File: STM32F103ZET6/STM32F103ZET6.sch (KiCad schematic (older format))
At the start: 0 parts

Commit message: git ignore STM32F103ZET6/STM32F103ZET6.sch-bak
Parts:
- added U?: STM32F103ZETx, Package_QFP:LQFP-144_20x20mm_P0.5mm, symbol MCU_ST_STM32F1:STM32F103ZETx
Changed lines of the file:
@@
 Comment4 ""
 $EndDescr
+$Comp
+L MCU_ST_STM32F1:STM32F103ZETx U?
+U 1 1 5E0CBF09
+P 5900 4000
+F 0 "U?" V 5854 357 50  0000 R CNN
+F 1 "STM32F103ZETx" V 5945 357 50  0000 R CNN
+F 2 "Package_QFP:LQFP-144_20x20mm_P0.5mm" H 4800 600 50  0001 R CNN
+F 3 "http://www.st.com/st-web-ui/static/active/en/resource/technical/document/datasheet/CD00191185.pdf" H 5900 4000 50  0001 C CNN
+	1    5900 4000
+	0    1    1    0
+$EndComp
 $EndSCHEMATC

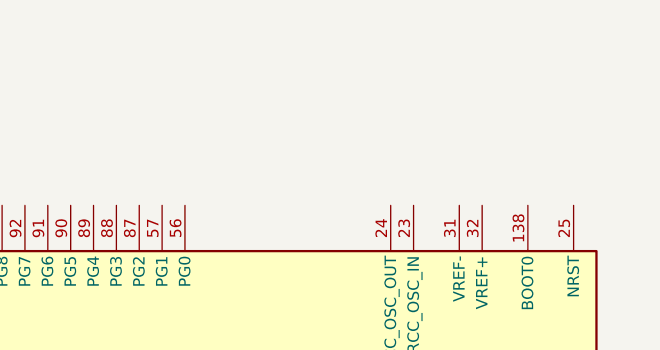
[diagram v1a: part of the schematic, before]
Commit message: remove STM32F103ZET6-cache.lib
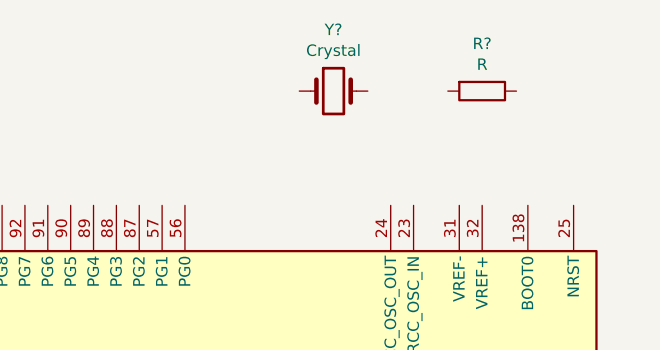
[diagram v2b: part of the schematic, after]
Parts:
- added R?: R, symbol Device:R
- added Y?: Crystal, symbol Device:Crystal
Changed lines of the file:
@@
 	0    1    1    0
 $EndComp
+$Comp
+L Device:R R?
+U 1 1 5E0CC0E2
+P 8800 2200
+F 0 "R?" V 8593 2200 50  0000 C CNN
+F 1 "R" V 8684 2200 50  0000 C CNN
+F 2 "" V 8730 2200 50  0001 C CNN
+F 3 "~" H 8800 2200 50  0001 C CNN
+	1    8800 2200
+	0    1    1    0
+$EndComp
+$Comp
+L Device:Crystal Y?
+U 1 1 5E0CC898
+P 8150 2200
+F 0 "Y?" H 8150 2468 50  0000 C CNN
+F 1 "Crystal" H 8150 2377 50  0000 C CNN
+F 2 "" H 8150 2200 50  0001 C CNN
+F 3 "~" H 8150 2200 50  0001 C CNN
+	1    8150 2200
+	1    0    0    -1
+$EndComp
 $EndSCHEMATC

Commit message: remove fp-info-cache
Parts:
- removed R?: R, symbol Device:R
- removed Y?: Crystal, symbol Device:Crystal
- gave numbers to parts that had none: 1
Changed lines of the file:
@@
 $EndDescr
 $Comp
-L MCU_ST_STM32F1:STM32F103ZETx U?
+L MCU_ST_STM32F1:STM32F103ZETx U1
 U 1 1 5E0CBF09
 P 5900 4000
-F 0 "U?" V 5854 357 50  0000 R CNN
+F 0 "U1" V 5854 357 50  0000 R CNN
 F 1 "STM32F103ZETx" V 5945 357 50  0000 R CNN
 F 2 "Package_QFP:LQFP-144_20x20mm_P0.5mm" H 4800 600 50  0001 R CNN
@@
 	0    1    1    0
 $EndComp
-$Comp
-L Device:R R?
-U 1 1 5E0CC0E2
-P 8800 2200
-F 0 "R?" V 8593 2200 50  0000 C CNN
-F 1 "R" V 8684 2200 50  0000 C CNN
-F 2 "" V 8730 2200 50  0001 C CNN
-F 3 "~" H 8800 2200 50  0001 C CNN
-	1    8800 2200
-	0    1    1    0
-$EndComp
-$Comp
-L Device:Crystal Y?
-U 1 1 5E0CC898
-P 8150 2200
-F 0 "Y?" H 8150 2468 50  0000 C CNN
-F 1 "Crystal" H 8150 2377 50  0000 C CNN
-F 2 "" H 8150 2200 50  0001 C CNN
-F 3 "~" H 8150 2200 50  0001 C CNN
-	1    8150 2200
-	1    0    0    -1
-$EndComp
 $EndSCHEMATC
